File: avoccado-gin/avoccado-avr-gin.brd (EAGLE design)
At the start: 42 x 17.5 mm, 61 parts, among them Q1 16MHz, Q2 FET, U1 MPU-6000QFN-24, U2 MCP73831

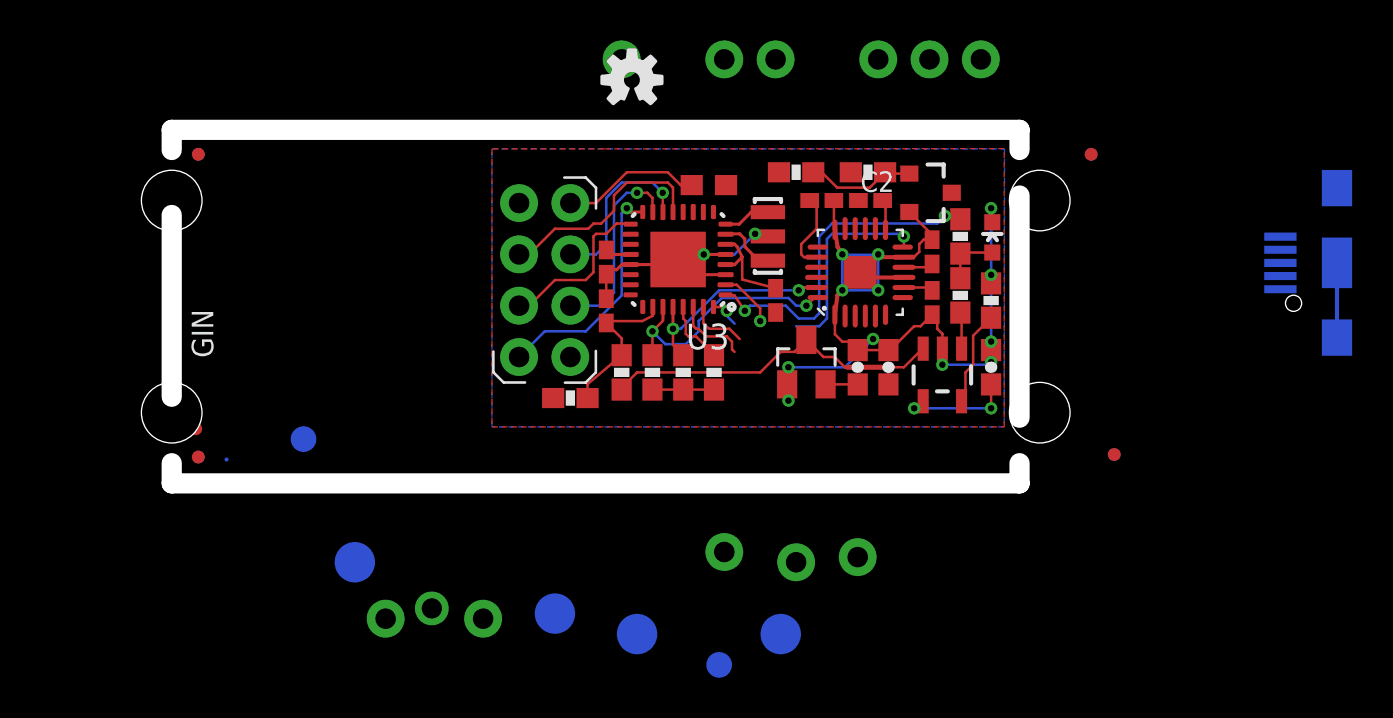
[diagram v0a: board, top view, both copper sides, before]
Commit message: add USB socket (without data lines)
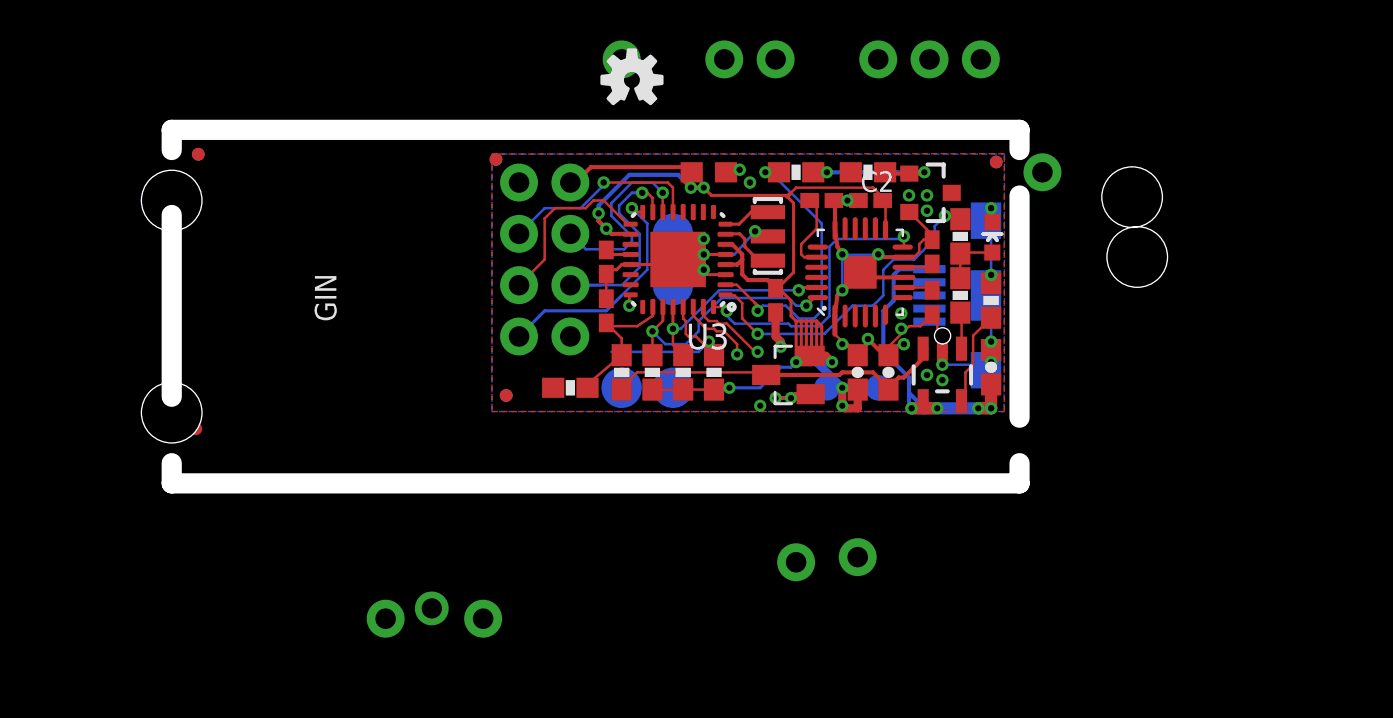
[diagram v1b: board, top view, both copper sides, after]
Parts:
- moved FID2 29.5 mm to (37.5, 36.7)
- moved FID8 29.5 mm to (37.5, 36.7)
- moved TP3 28.6 mm to (56.4, 25.4)
- moved JP23 24.5 mm to (64.5, 36.1)
- moved TP12 22.6 mm to (46.2, 33.0)
- moved JP22 17.4 mm to (61.7, 30.0)
- moved TP13 17.3 mm to (46.2, 30.5)
- moved FID5 15.6 mm to (62.2, 36.6)
- moved FID9 15.6 mm to (62.2, 36.6)
- moved FID4 15.5 mm to (38.0, 25.0)
- moved FID6 15.5 mm to (38.0, 25.0)
- moved TP5 14.7 mm to (53.8, 25.4)
- moved TP4 14.5 mm to (43.7, 25.4)
- moved TP10 12.3 mm to (46.2, 25.4)
- moved LDO 1.09 mm to (51.9, 26.0), turned to 90 degrees
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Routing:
- net 3.3V: track 18.0 -> 71.3 mm, vias 0 -> 9
- net 5V: track 5.58 -> 18.1 mm, vias 2 -> 4
- net D4: track 2.83 -> 14.8 mm, vias 1 -> 2
- net GND: track 74.1 -> 64.2 mm, vias 14 -> 29
- net RESET: track 3.23 -> 9.05 mm, vias 0 -> 1
- net D2-INT: track 11.7 -> 14.4 mm
- net N$6: track 5.41 -> 7.92 mm, vias 0 -> 2
- net D10: track 8.55 -> 9.98 mm
- net TXO: track 2.93 -> 3.86 mm, vias 0 -> 1
- net D9: track 10.9 -> 10.0 mm, vias 0 -> 1
- net SCK: track 8.26 -> 8.94 mm
- net VBAT: track 17.8 -> 17.1 mm
- net A1: track 0.00 -> 0.56 mm, vias 0 -> 1
- net RXI: track 3.74 -> 3.69 mm, vias 0 -> 1
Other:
- board text removed: "5"
- board text removed: "G"

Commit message: cleanup unused headers
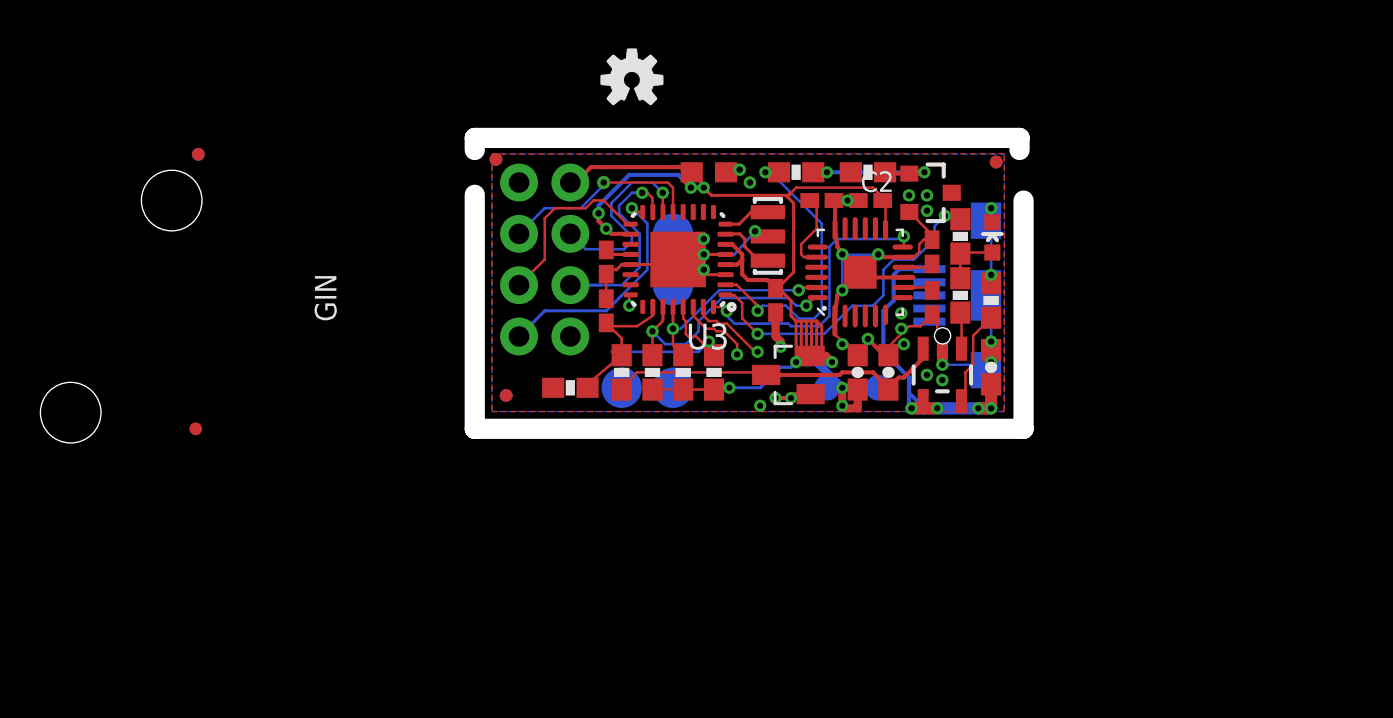
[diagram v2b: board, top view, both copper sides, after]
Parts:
- removed JP17, JP18, JP19, JP21, JP23, JP24, JP25, JP3, JP6, JP8, JP9: M01PTH, SparkFun-Connectors:1X01
- removed JP20: M01NOSILK-KIT, SparkFun-Connectors:1X01NS-KIT
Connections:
- net 3.3V: no longer JP18.1
- net 5V: no longer JP17.1
- net A0: no longer JP19.1
- net A1: no longer JP20.1
- net A2: no longer JP21.1
- net GND: no longer JP25.1, JP3.1, JP6.1
- net RXI: no longer JP8.1
- net TXO: no longer JP9.1
- net VBAT: no longer JP24.1
- net VIBR: no longer JP23.1
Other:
- board size 42 x 17.5 mm -> 27.2 x 14.4 mm

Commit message: add RX and TX test points
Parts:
- added TP1, TP2, TP6, TP7, TP8: TPTP20R, testpad:TP20R
- moved TP4 12.7 mm to (56.4, 25.4)
- moved TP3 8.40 mm to (64.8, 24.9), turned to 180 degrees
- moved TP13 5.62 mm to (48.6, 35.6)
- moved TP10 2.54 mm to (43.7, 25.4)
- moved FID5 2.30 mm to (59.9, 36.3)
- moved FID9 2.30 mm to (59.9, 36.3)
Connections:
- net A1: now also TP8.TP
- net A7-NRF-IRQ: no longer JP29.2
- net RESET: now also TP7.TP
- net RXI: now also TP2.TP
- net TXO: now also TP6.TP
- net VIBR: now also TP1.TP
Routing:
- net RXI: track 3.69 -> 7.48 mm
- net TXO: track 3.86 -> 6.32 mm
- net VBAT: track 17.1 -> 18.8 mm, vias 0 -> 2
- net VIBR: track 0.00 -> 1.65 mm
- net 3.3V: track 71.3 -> 73.0 mm
- net D10: track 9.98 -> 8.79 mm
- net MOSI: track 9.99 -> 8.83 mm
- net A1: track 0.56 -> 1.70 mm
- net GND: vias 29 -> 32

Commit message: no airwires left :shipit:
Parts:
- added TP9: TPTP20R, testpad:TP20R
- moved TP3 13.5 mm to (51.3, 25.4)
- moved TP12 7.62 mm to (46.2, 25.4)
- moved TP2 7.62 mm to (38.6, 25.4)
- moved TP6 7.62 mm to (41.1, 25.4)
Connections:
- net 3.3V: now also TP9.TP
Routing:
- net GND: track 64.2 -> 91.2 mm, vias 32 -> 33
- net RXI: track 7.48 -> 15.0 mm
- net TXO: track 6.32 -> 13.9 mm
- net 3.3V: track 73.0 -> 71.1 mm

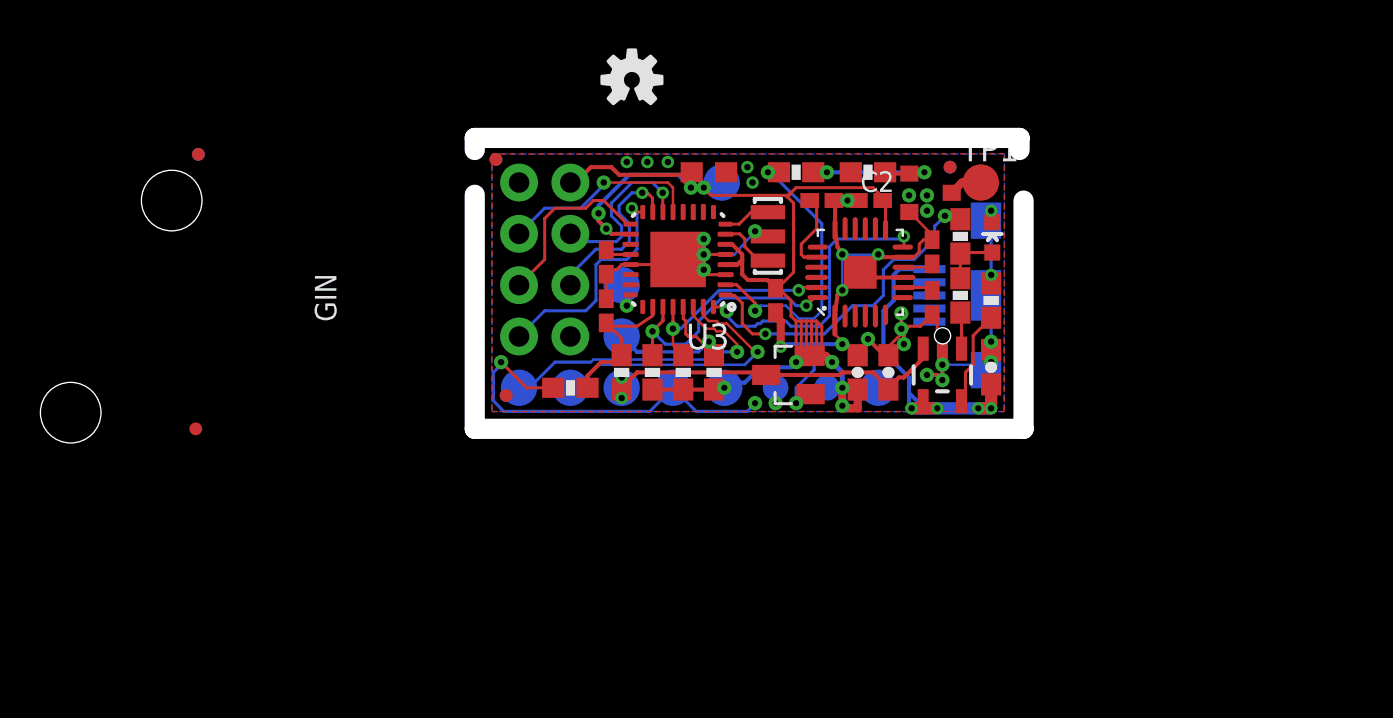
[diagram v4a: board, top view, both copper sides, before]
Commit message: add SMD pads to bottom layer
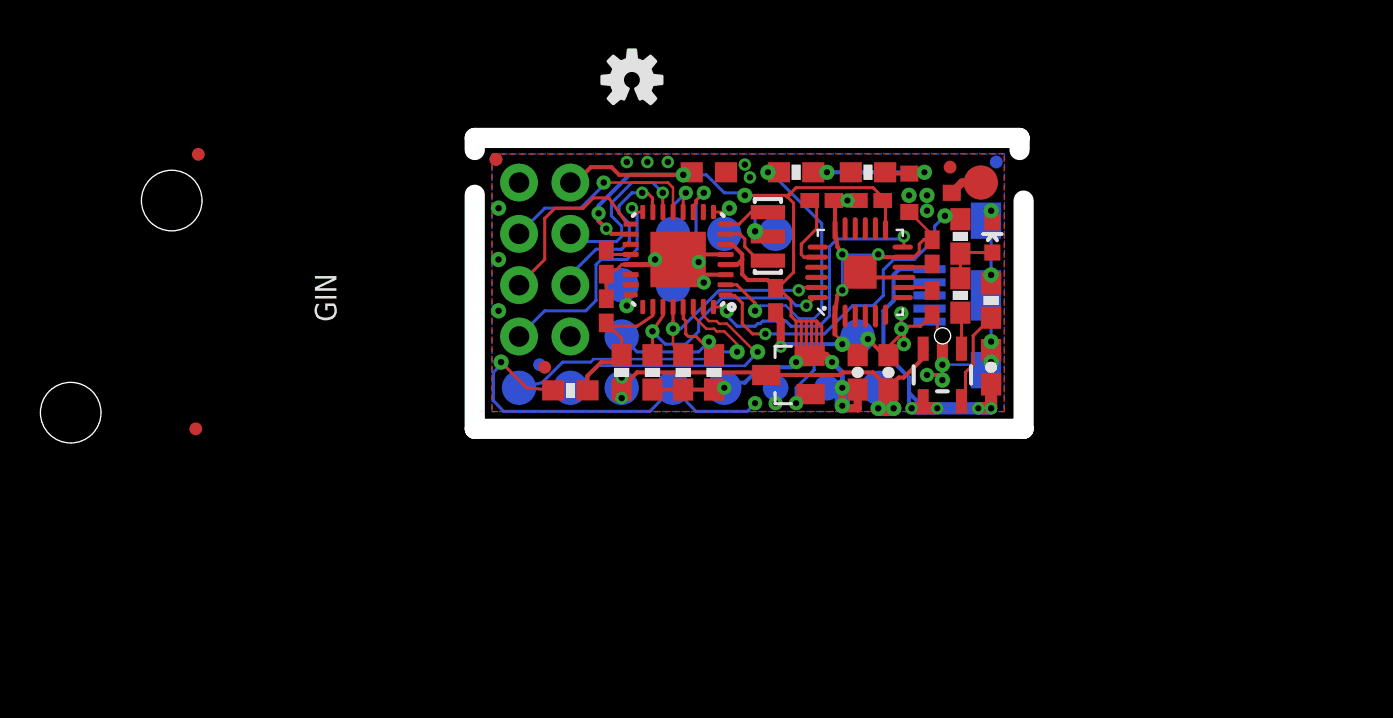
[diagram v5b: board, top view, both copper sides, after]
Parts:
- removed FID7: FIDUCIALUFIDUCIAL, SparkFun-Aesthetics:MICRO-FIDUCIAL
- removed TP13: TPTP20R, testpad:TP20R
- added TP11, TP14, TP15, TP16, TP17: TPTP20R, testpad:TP20R
- moved FID4 2.36 mm to (39.9, 26.4)
- moved FID9 2.30 mm to (62.2, 36.6)
- moved FID6 2.25 mm to (39.6, 26.5)
- moved R7 0.13 mm to (41.1, 25.3)
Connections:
- net 3.3V: no longer TP13.TP
- net D5: now also TP15.TP
- net D7: now also TP14.TP
- net D8: now also TP11.TP
- net GND: now also TP16.TP, TP17.TP; no longer TP4.TP
- net VBAT: now also TP4.TP
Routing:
- net D7: track 0.00 -> 6.37 mm, vias 0 -> 1
- net VBAT: track 18.8 -> 22.7 mm, vias 2 -> 4
- net D8: track 0.00 -> 3.28 mm, vias 0 -> 1
- net 3.3V: track 71.1 -> 68.0 mm
- net D5: track 0.00 -> 2.24 mm, vias 0 -> 1
- net GND: track 91.2 -> 91.8 mm, vias 33 -> 36
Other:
- board text added: "3V3"
- board text added: "5"
- board text added: "A1"
- board text added: "BAT"
- board text added: "GND"
- board text added: "RXI"
- board text added: "TXO"
- board text removed: "5V"
- board text removed: "6"
- board text removed: "CK"
- board text removed: "D4"
- board text removed: "DT"
- board text removed: "GN"
- board text removed: "MI"
- board text removed: "MO"
- board text removed: "RX"
- board text removed: "TX"
- board text removed: "VC"

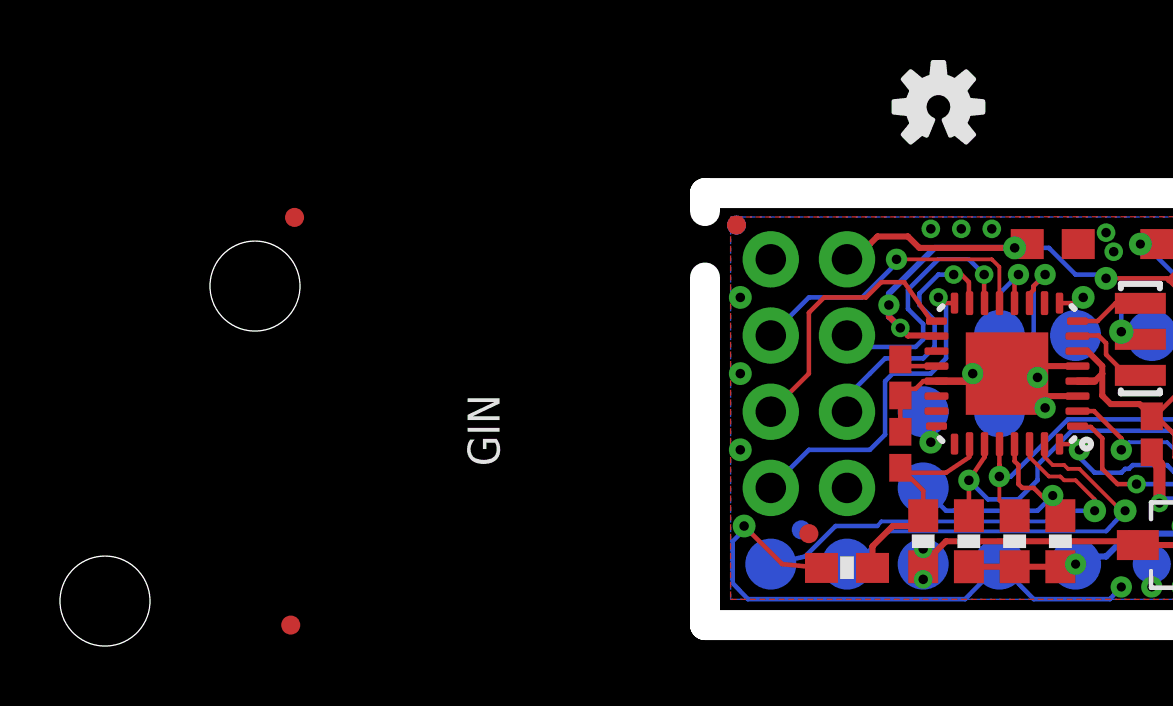
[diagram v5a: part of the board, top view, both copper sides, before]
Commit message: Finish silkscreen with a wide A° instead of pin declarations
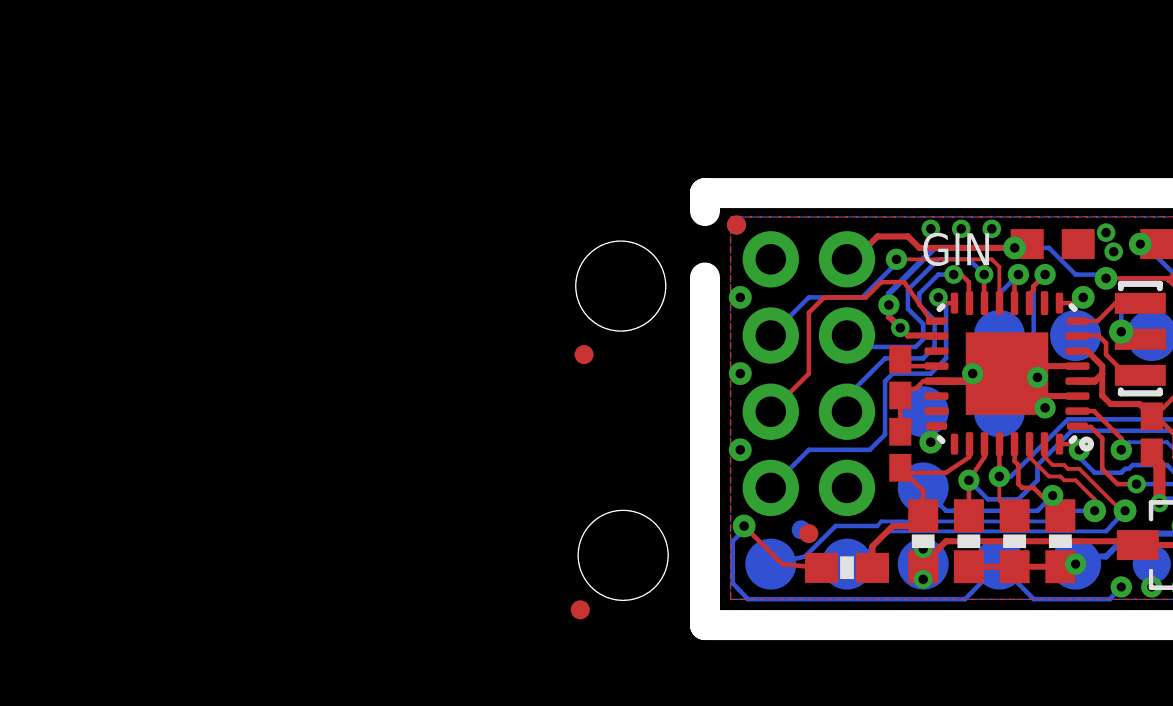
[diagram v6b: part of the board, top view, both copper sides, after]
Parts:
- removed LOGO1: OSHW-LOGOS, SparkFun-Aesthetics:OSHW-LOGO-S
- moved FID1 10.7 mm to (32.4, 32.4)
- moved FID3 9.67 mm to (32.3, 23.9)
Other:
- board text added: "AVOCCADO GIN"
- board text removed: "3V3"
- board text removed: "5"
- board text removed: "7"
- board text removed: "8"
- board text removed: "A1"
- board text removed: "AVOCCADO.CC"
- board text removed: "BAT"
- board text removed: "GND"
- board text removed: "LIPO"
- board text removed: "RS"
- board text removed: "RXI"
- board text removed: "TXO"

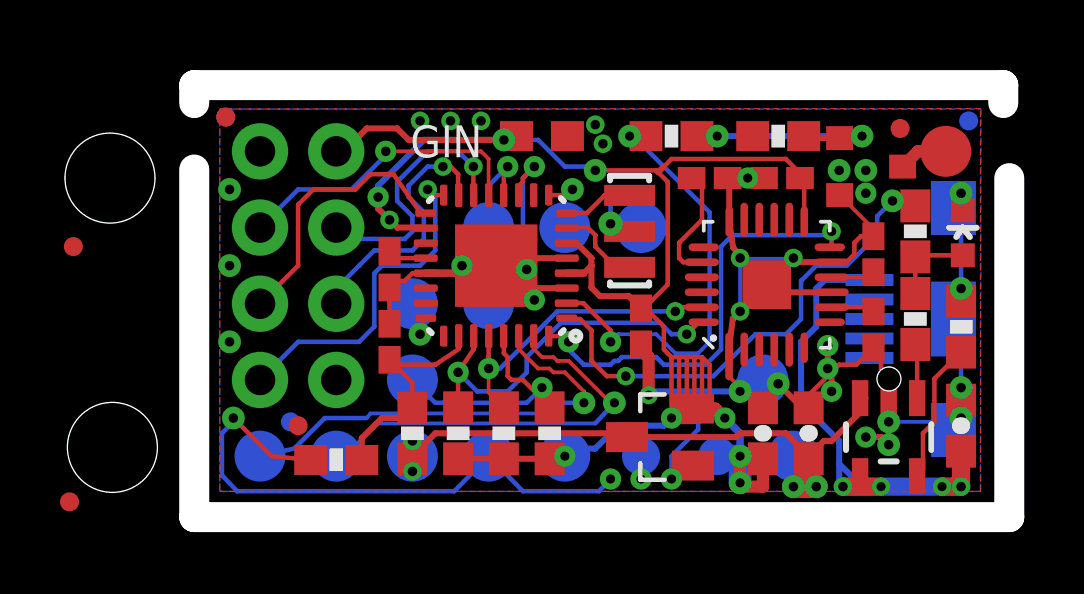
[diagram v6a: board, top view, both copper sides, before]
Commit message: render PNG preview
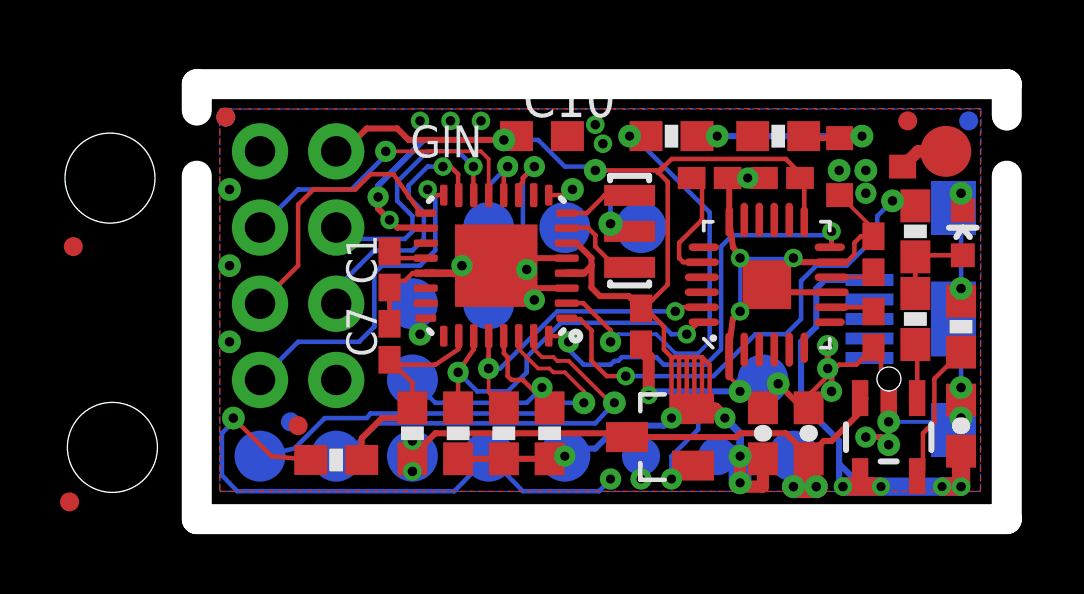
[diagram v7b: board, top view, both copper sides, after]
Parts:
- C10: value 0.1uF -> 4.7uF
- Q2: value FET -> N-FET
- moved FID5 0.36 mm to (60.2, 36.6)
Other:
- board size 27.2 x 14.4 mm -> 27 x 14.5 mm

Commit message: DRC check with 6mil / 6mil, silkscreen touchup
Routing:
- net GND: track 91.8 -> 93.8 mm, vias 36 -> 35
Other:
- board text added: "OCC DO GIN"
- board text removed: "AVOCCADO GIN"
